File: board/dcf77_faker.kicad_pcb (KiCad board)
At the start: 4 copper layers, 69 x 32 mm, 50 parts, among them J1 Barrel_Jack, J2 DBG, J3 ANT, J4 LCD_I2C, SW1 RST, SW2 H, SW3 MIN, SW4 S, U1 NCP1117ST33T3G, U2 ATSAML21G18B-AUT, X1 32.768kHz, X2 31MHz

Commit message: board: slight PCB tweaks, more info
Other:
- board text added: "https://github.com/RavuAlHemio/dcf77-faker"
- board text added: "r0001"
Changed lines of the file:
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@@
     (fp_line (start -1.6 -0.4) (end -1.6 0.8) (layer "F.Fab") (width 0.1))
     (fp_line (start 1.6 -0.8) (end -1.2 -0.8) (layer "F.Fab") (width 0.1))
-    (pad "1" smd roundrect (at -1.35 0 90) (size 1.4 1.35) (layers "F.Cu" "F.Paste" "F.Mask") (roundrect_rratio 0.185185)
+    (pad "1" smd roundrect (at -1.35 0 90) (size 1.4 1.35) (layers "F.Cu" "F.Paste" "F.Mask") (roundrect_rratio 0.1851851852)
       (net 3 "+3.3V") (pintype "passive"))
-    (pad "2" smd roundrect (at 1.35 0 90) (size 1.4 1.35) (layers "F.Cu" "F.Paste" "F.Mask") (roundrect_rratio 0.185185)
+    (pad "2" smd roundrect (at 1.35 0 90) (size 1.4 1.35) (layers "F.Cu" "F.Paste" "F.Mask") (roundrect_rratio 0.1851851852)
       (net 7 "/RAWGND") (pintype "passive"))
     (model "${KICAD6_3DMODEL_DIR}/Capacitor_Tantalum_SMD.3dshapes/CP_EIA-3216-18_Kemet-A.wrl"
@@
     (fp_line (start 1.6 -0.8) (end 1.6 0.8) (layer "F.Fab") (width 0.1))
     (fp_line (start -1.6 -0.8) (end 1.6 -0.8) (layer "F.Fab") (width 0.1))
-    (pad "1" smd roundrect (at -1.575 0 270) (size 1.05 1.9) (layers "F.Cu" "F.Paste" "F.Mask") (roundrect_rratio 0.238095)
+    (pad "1" smd roundrect (at -1.575 0 270) (size 1.05 1.9) (layers "F.Cu" "F.Paste" "F.Mask") (roundrect_rratio 0.2380952381)
       (net 8 "/VDDCORE") (pinfunction "1") (pintype "passive"))
-    (pad "2" smd roundrect (at 1.575 0 270) (size 1.05 1.9) (layers "F.Cu" "F.Paste" "F.Mask") (roundrect_rratio 0.238095)
+    (pad "2" smd roundrect (at 1.575 0 270) (size 1.05 1.9) (layers "F.Cu" "F.Paste" "F.Mask") (roundrect_rratio 0.2380952381)
       (net 9 "/VSW") (pinfunction "2") (pintype "passive"))
     (model "${KICAD6_3DMODEL_DIR}/Inductor_SMD.3dshapes/L_1206_3216Metric.wrl"
@@
     (fp_line (start 1.6 0.8) (end -1.6 0.8) (layer "F.Fab") (width 0.1))
     (fp_line (start -1.6 -0.8) (end 1.6 -0.8) (layer "F.Fab") (width 0.1))
-    (pad "1" smd roundrect (at -1.575 0 180) (size 1.05 1.9) (layers "F.Cu" "F.Paste" "F.Mask") (roundrect_rratio 0.238095)
+    (pad "1" smd roundrect (at -1.575 0 180) (size 1.05 1.9) (layers "F.Cu" "F.Paste" "F.Mask") (roundrect_rratio 0.2380952381)
       (net 48 "/VDDIN") (pinfunction "1") (pintype "passive"))
-    (pad "2" smd roundrect (at 1.575 0 180) (size 1.05 1.9) (layers "F.Cu" "F.Paste" "F.Mask") (roundrect_rratio 0.238095)
+    (pad "2" smd roundrect (at 1.575 0 180) (size 1.05 1.9) (layers "F.Cu" "F.Paste" "F.Mask") (roundrect_rratio 0.2380952381)
       (net 4 "/VDDANA") (pinfunction "2") (pintype "passive"))
     (model "${KICAD6_3DMODEL_DIR}/Inductor_SMD.3dshapes/L_1206_3216Metric.wrl"
@@
     (fp_line (start -1.2 -0.8) (end -1.6 -0.4) (layer "F.Fab") (width 0.1))
     (fp_line (start -1.6 0.8) (end 1.6 0.8) (layer "F.Fab") (width 0.1))
-    (pad "1" smd roundrect (at -1.35 0 90) (size 1.4 1.35) (layers "F.Cu" "F.Paste" "F.Mask") (roundrect_rratio 0.185185)
+    (pad "1" smd roundrect (at -1.35 0 90) (size 1.4 1.35) (layers "F.Cu" "F.Paste" "F.Mask") (roundrect_rratio 0.1851851852)
       (net 2 "Net-(C1-Pad1)") (pintype "passive"))
-    (pad "2" smd roundrect (at 1.35 0 90) (size 1.4 1.35) (layers "F.Cu" "F.Paste" "F.Mask") (roundrect_rratio 0.185185)
+    (pad "2" smd roundrect (at 1.35 0 90) (size 1.4 1.35) (layers "F.Cu" "F.Paste" "F.Mask") (roundrect_rratio 0.1851851852)
       (net 7 "/RAWGND") (pintype "passive"))
     (model "${KICAD6_3DMODEL_DIR}/Capacitor_Tantalum_SMD.3dshapes/CP_EIA-3216-18_Kemet-A.wrl"
@@
       ) (layer "F.SilkS") (width 0) (fill solid))
   )
-  (gr_line (start 158.6 81.3) (end 160.6 81.3) (layer "F.SilkS") (width 0.15))
-  (gr_arc (start 159.3 82) (mid 157.610051 81.3) (end 159.3 80.6) (layer "F.SilkS") (width 0.15))
-  (gr_line (start 155.1 81.3) (end 156.1 81.3) (layer "F.SilkS") (width 0.15))
-  (gr_circle (center 158.6 81.3) (end 159.1 81.3) (layer "F.SilkS") (width 0.15) (fill solid))
-  (gr_line (start 161.6 81.8) (end 161.6 80.8) (layer "F.SilkS") (width 0.15))
-  (gr_circle (center 161.6 81.3) (end 162.6 81.3) (layer "F.SilkS") (width 0.15) (fill none))
-  (gr_line (start 156.6 81.3) (end 157.610051 81.3) (layer "F.SilkS") (width 0.15))
-  (gr_line (start 161.1 81.3) (end 162.1 81.3) (layer "F.SilkS") (width 0.15))
-  (gr_circle (center 155.6 81.3) (end 156.6 81.3) (layer "F.SilkS") (width 0.15) (fill none))
+  (gr_line (start 159.1 81.3) (end 161.1 81.3) (layer "F.SilkS") (width 0.15))
+  (gr_arc (start 159.8 82) (mid 158.110051 81.3) (end 159.8 80.6) (layer "F.SilkS") (width 0.15))
+  (gr_line (start 155.6 81.3) (end 156.6 81.3) (layer "F.SilkS") (width 0.15))
+  (gr_circle (center 159.1 81.3) (end 159.6 81.3) (layer "F.SilkS") (width 0.15) (fill solid))
+  (gr_line (start 162.1 81.8) (end 162.1 80.8) (layer "F.SilkS") (width 0.15))
+  (gr_circle (center 162.1 81.3) (end 163.1 81.3) (layer "F.SilkS") (width 0.15) (fill none))
+  (gr_line (start 157.1 81.3) (end 158.110051 81.3) (layer "F.SilkS") (width 0.15))
+  (gr_line (start 161.6 81.3) (end 162.6 81.3) (layer "F.SilkS") (width 0.15))
+  (gr_circle (center 156.1 81.3) (end 157.1 81.3) (layer "F.SilkS") (width 0.15) (fill none))
   (gr_line (start 150 60) (end 150 86) (layer "Edge.Cuts") (width 0.1))
   (gr_arc (start 219 86) (mid 218.12132 88.12132) (end 216 89) (layer "Edge.Cuts") (width 0.1))
@@
   (gr_arc (start 216 57) (mid 218.12132 57.87868) (end 219 60) (layer "Edge.Cuts") (width 0.1))
   (gr_arc (start 153 89) (mid 150.87868 88.12132) (end 150 86) (layer "Edge.Cuts") (width 0.1))
-  (gr_text "rec 12V, max 20V" (at 158.8 79) (layer "F.SilkS")
+  (gr_text "https://github.com/RavuAlHemio/dcf77-faker" (at 169.164 78.994) (layer "B.SilkS")
+    (effects (font (size 1 1) (thickness 0.15)) (justify mirror))
+  )
+  (gr_text "rec 12V, max 20V" (at 159.258 78.994) (layer "F.SilkS")
     (effects (font (size 1 1) (thickness 0.15)))
   )
@@
     (effects (font (size 1 1) (thickness 0.15)))
   )
+  (gr_text "r0001" (at 159.258 86.36) (layer "F.SilkS")
+    (effects (font (size 1 1) (thickness 0.15)))
+  )

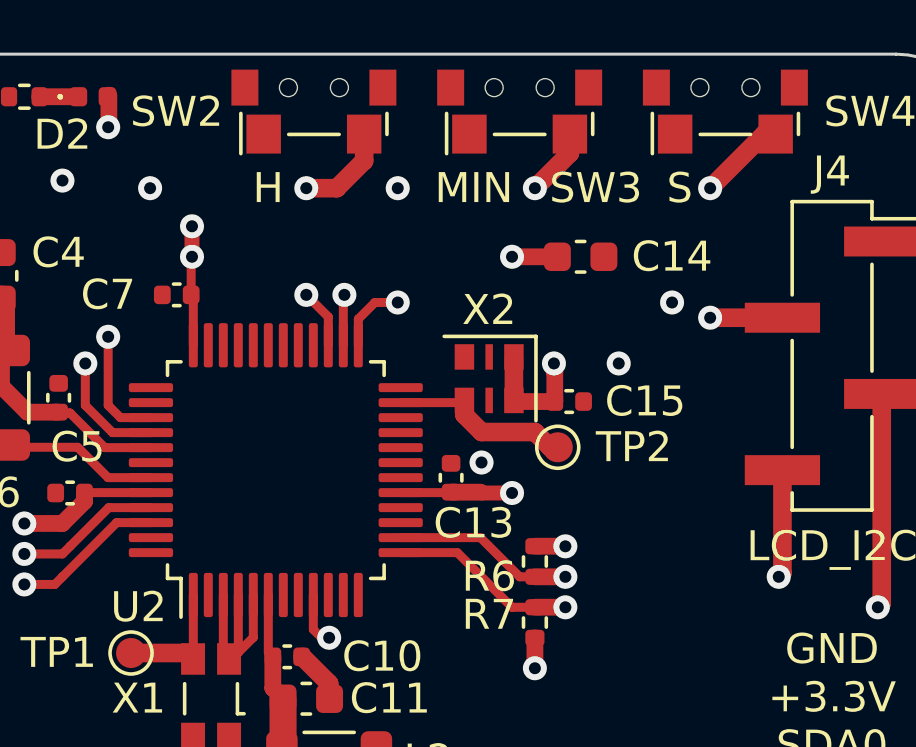
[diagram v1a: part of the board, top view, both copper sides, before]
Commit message: board: replace X2 with 7x5mm footprint (Microchip DSC8001A)
this should make it easier to hand-solder after programming
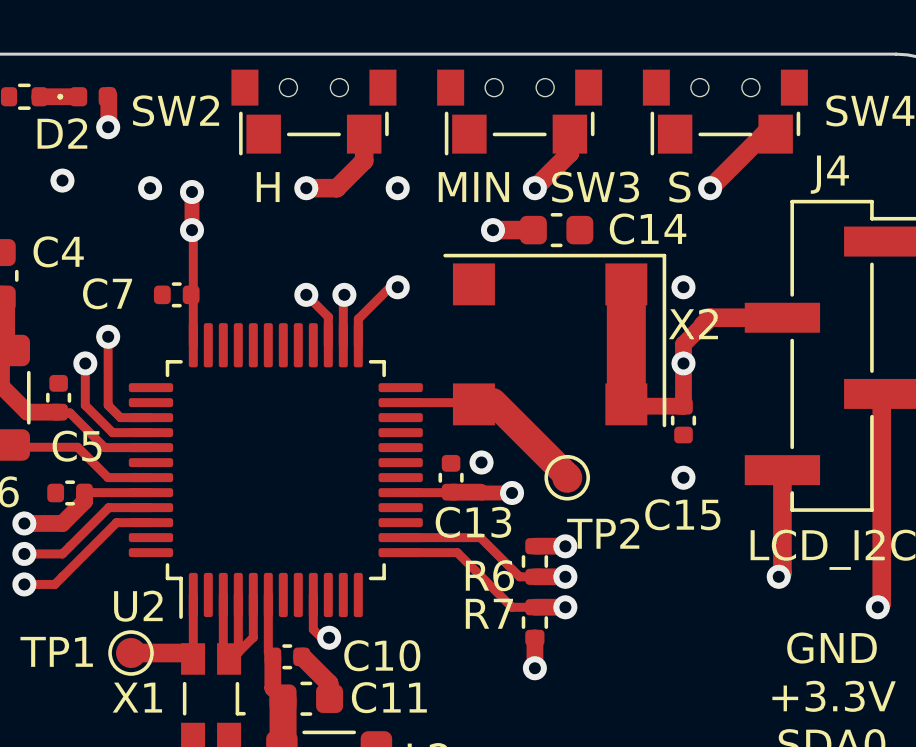
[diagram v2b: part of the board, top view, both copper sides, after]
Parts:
- X2: footprint Oscillator_Microchip:Oscillator_SMD_Microchip_DSC1101D-6Pin_2.5x2.0mm -> Oscillator_Microchip:Oscillator_SMD_Microchip_DSC8001A-6Pin_7.0x5.0mm
- moved C15 3.86 mm to (208.9, 69.2), turned to 90 degrees
- moved X2 2.33 mm to (204.5, 66.7)
- moved C14 1.20 mm to (204.7, 62.9)
- moved TP2 1.06 mm to (205.0, 71.1)
- moved NT2 1.02 mm to (192.5, 62.2)
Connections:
- X2 pad 2: unconnected-(X2-Pad2) -> GND
- X2 pad 3: GND -> /XIN
- X2 pad 4: /XIN -> +3.3V
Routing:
- net +3.3V: track 32.5 -> 37.9 mm, vias 12 -> 11
- net /VDDIO2: track 23.0 -> 24.2 mm
